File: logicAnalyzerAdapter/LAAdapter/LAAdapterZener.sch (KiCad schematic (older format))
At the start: 13 parts, among them J1 Conn_01x02_Male, J10 Conn_01x01_Female, J2 Conn_01x02_Male, J3 Conn_01x02_Male, J4 Conn_01x02_Male, J5 Conn_02x05_Odd_Even, J6 Conn_01x02_Male, J7 Conn_01x02_Male, J8 Conn_01x02_Male, J9 Conn_01x01_Female

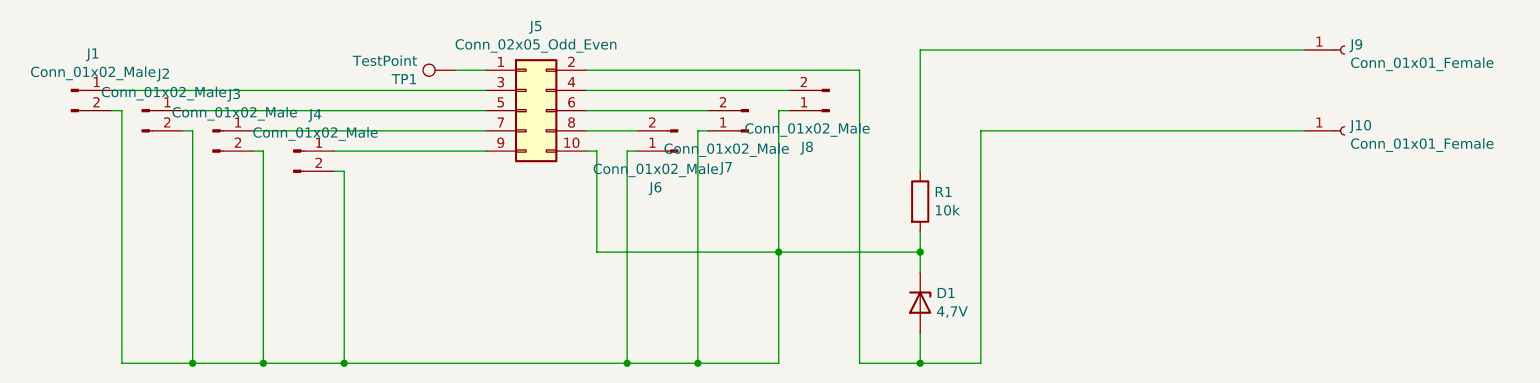
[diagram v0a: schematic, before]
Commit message: opravena hrubá chyba
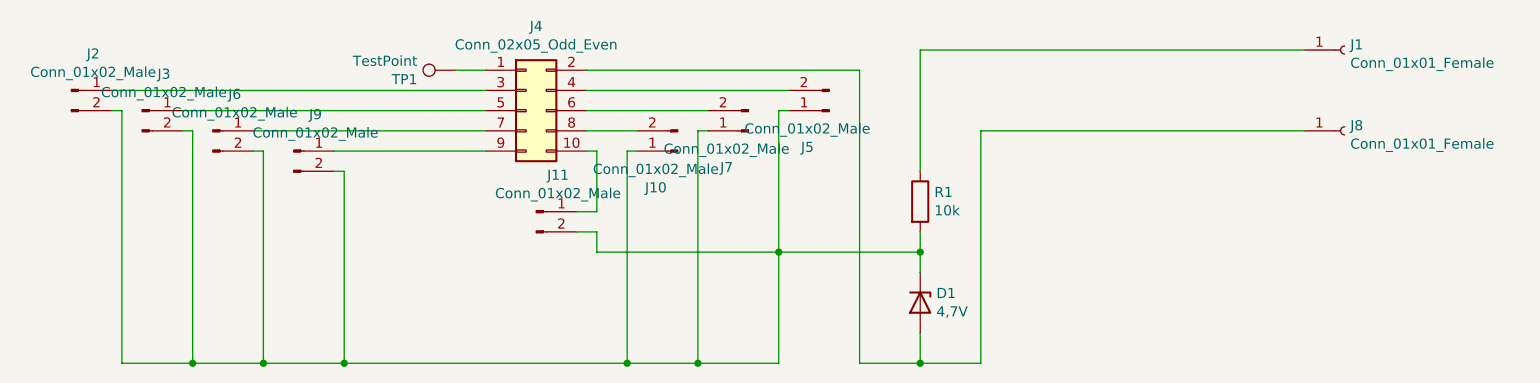
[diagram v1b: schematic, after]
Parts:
- added J11: Conn_01x02_Male, Jumper:SolderJumper-2_P1.3mm_Open_Pad1.0x1.5mm, symbol Connector:Conn_01x02_Male
- J10: renamed from J6; footprint Jumper:SolderJumper-2_P1.3mm_Open_TrianglePad1.0x1.5mm -> Jumper:SolderJumper-2_P1.3mm_Open_Pad1.0x1.5mm
- J2: renamed from J1; footprint Jumper:SolderJumper-2_P1.3mm_Open_TrianglePad1.0x1.5mm -> Jumper:SolderJumper-2_P1.3mm_Open_Pad1.0x1.5mm
- J3: renamed from J2; footprint Jumper:SolderJumper-2_P1.3mm_Open_TrianglePad1.0x1.5mm -> Jumper:SolderJumper-2_P1.3mm_Open_Pad1.0x1.5mm
- J5: renamed from J8; footprint Jumper:SolderJumper-2_P1.3mm_Open_TrianglePad1.0x1.5mm -> Jumper:SolderJumper-2_P1.3mm_Open_Pad1.0x1.5mm
- J6: renamed from J3; footprint Jumper:SolderJumper-2_P1.3mm_Open_TrianglePad1.0x1.5mm -> Jumper:SolderJumper-2_P1.3mm_Open_Pad1.0x1.5mm
- J7: footprint Jumper:SolderJumper-2_P1.3mm_Open_TrianglePad1.0x1.5mm -> Jumper:SolderJumper-2_P1.3mm_Open_Pad1.0x1.5mm
- J9: renamed from J4; footprint Jumper:SolderJumper-2_P1.3mm_Open_TrianglePad1.0x1.5mm -> Jumper:SolderJumper-2_P1.3mm_Open_Pad1.0x1.5mm
- renumbered J9 to J1, J5 to J4, J10 to J8
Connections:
- net at D1.1 (K), J10.1 (Pin_1), J2.2 (Pin_2)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: now also J11.2 (Pin_2); no longer J4.10 (Pin_10)
- new net: J11.1 (Pin_1), J4.10 (Pin_10)
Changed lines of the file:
@@
 $EndComp
 $Comp
-L Connector_Generic:Conn_02x05_Odd_Even J5
+L Connector_Generic:Conn_02x05_Odd_Even J4
 U 1 1 60510CB1
 P 3100 3250
-F 0 "J5" H 3150 3667 50  0000 C CNN
+F 0 "J4" H 3150 3667 50  0000 C CNN
 F 1 "Conn_02x05_Odd_Even" H 3150 3576 50  0000 C CNN
 F 2 "AR_Library:AR_PinHeader_2x05_P2.54mm_Horizontal" H 3100 3250 50  0001 C CNN
@@
 $EndComp
 $Comp
-L Connector:Conn_01x01_Female J10
+L Connector:Conn_01x01_Female J8
 U 1 1 6051A2D4
 P 7150 3350
-F 0 "J10" H 7178 3376 50  0000 L CNN
+F 0 "J8" H 7178 3376 50  0000 L CNN
 F 1 "Conn_01x01_Female" H 7178 3285 50  0000 L CNN
 F 2 "AR_Library:AR_AMASS_4mm_Horizontal" H 7150 3350 50  0001 C CNN
@@
 $EndComp
 $Comp
-L Connector:Conn_01x01_Female J9
+L Connector:Conn_01x01_Female J1
 U 1 1 6051AB13
 P 7150 2950
-F 0 "J9" H 7178 2976 50  0000 L CNN
+F 0 "J1" H 7178 2976 50  0000 L CNN
 F 1 "Conn_01x01_Female" H 7178 2885 50  0000 L CNN
 F 2 "AR_Library:AR_AMASS_4mm_Horizontal" H 7150 2950 50  0001 C CNN
@@
 Wire Wire Line
 	4750 4500 5050 4500
-Wire Wire Line
-	3400 3050 4750 3050
 Connection ~ 5050 4500
 $Comp
-L Connector:Conn_01x02_Male J1
+L Connector:Conn_01x02_Male J2
 U 1 1 60531B24
 P 850 3150
-F 0 "J1" H 958 3331 50  0000 C CNN
+F 0 "J2" H 958 3331 50  0000 C CNN
 F 1 "Conn_01x02_Male" H 958 3240 50  0000 C CNN
-F 2 "Jumper:SolderJumper-2_P1.3mm_Open_TrianglePad1.0x1.5mm" H 850 3150 50  0001 C CNN
+F 2 "Jumper:SolderJumper-2_P1.3mm_Open_Pad1.0x1.5mm" H 850 3150 50  0001 C CNN
 F 3 "~" H 850 3150 50  0001 C CNN
 	1    850  3150
@@
 	5050 3950 5050 4050
 $Comp
-L Connector:Conn_01x02_Male J2
+L Connector:Conn_01x02_Male J3
 U 1 1 60534A19
 P 1200 3250
-F 0 "J2" H 1308 3431 50  0000 C CNN
+F 0 "J3" H 1308 3431 50  0000 C CNN
 F 1 "Conn_01x02_Male" H 1308 3340 50  0000 C CNN
-F 2 "Jumper:SolderJumper-2_P1.3mm_Open_TrianglePad1.0x1.5mm" H 1200 3250 50  0001 C CNN
+F 2 "Jumper:SolderJumper-2_P1.3mm_Open_Pad1.0x1.5mm" H 1200 3250 50  0001 C CNN
 F 3 "~" H 1200 3250 50  0001 C CNN
 	1    1200 3250
@@
 $EndComp
 $Comp
-L Connector:Conn_01x02_Male J3
+L Connector:Conn_01x02_Male J6
 U 1 1 605352E5
 P 1550 3350
-F 0 "J3" H 1658 3531 50  0000 C CNN
+F 0 "J6" H 1658 3531 50  0000 C CNN
 F 1 "Conn_01x02_Male" H 1658 3440 50  0000 C CNN
-F 2 "Jumper:SolderJumper-2_P1.3mm_Open_TrianglePad1.0x1.5mm" H 1550 3350 50  0001 C CNN
+F 2 "Jumper:SolderJumper-2_P1.3mm_Open_Pad1.0x1.5mm" H 1550 3350 50  0001 C CNN
 F 3 "~" H 1550 3350 50  0001 C CNN
 	1    1550 3350
@@
 $EndComp
 $Comp
-L Connector:Conn_01x02_Male J4
+L Connector:Conn_01x02_Male J9
 U 1 1 605396F3
 P 1950 3450
-F 0 "J4" H 2058 3631 50  0000 C CNN
+F 0 "J9" H 2058 3631 50  0000 C CNN
 F 1 "Conn_01x02_Male" H 2058 3540 50  0000 C CNN
-F 2 "Jumper:SolderJumper-2_P1.3mm_Open_TrianglePad1.0x1.5mm" H 1950 3450 50  0001 C CNN
+F 2 "Jumper:SolderJumper-2_P1.3mm_Open_Pad1.0x1.5mm" H 1950 3450 50  0001 C CNN
 F 3 "~" H 1950 3450 50  0001 C CNN
 	1    1950 3450
@@
 	3400 3450 3450 3450
 Wire Wire Line
-	3450 3450 3450 3950
-Wire Wire Line
 	3450 3950 4350 3950
 $Comp
-L Connector:Conn_01x02_Male J8
+L Connector:Conn_01x02_Male J5
 U 1 1 6053DACB
 P 4600 3250
-F 0 "J8" H 4708 3431 50  0000 C CNN
+F 0 "J5" H 4708 3431 50  0000 C CNN
 F 1 "Conn_01x02_Male" H 4708 3340 50  0000 C CNN
-F 2 "Jumper:SolderJumper-2_P1.3mm_Open_TrianglePad1.0x1.5mm" H 4600 3250 50  0001 C CNN
+F 2 "Jumper:SolderJumper-2_P1.3mm_Open_Pad1.0x1.5mm" H 4600 3250 50  0001 C CNN
 F 3 "~" H 4600 3250 50  0001 C CNN
 	1    4600 3250
@@
 F 0 "J7" H 4308 3531 50  0000 C CNN
 F 1 "Conn_01x02_Male" H 4308 3440 50  0000 C CNN
-F 2 "Jumper:SolderJumper-2_P1.3mm_Open_TrianglePad1.0x1.5mm" H 4200 3350 50  0001 C CNN
+F 2 "Jumper:SolderJumper-2_P1.3mm_Open_Pad1.0x1.5mm" H 4200 3350 50  0001 C CNN
 F 3 "~" H 4200 3350 50  0001 C CNN
 	1    4200 3350
@@
 $EndComp
 $Comp
-L Connector:Conn_01x02_Male J6
+L Connector:Conn_01x02_Male J10
 U 1 1 6053F0C1
 P 3850 3450
-F 0 "J6" H 3958 3631 50  0000 C CNN
+F 0 "J10" H 3958 3631 50  0000 C CNN
 F 1 "Conn_01x02_Male" H 3958 3540 50  0000 C CNN
-F 2 "Jumper:SolderJumper-2_P1.3mm_Open_TrianglePad1.0x1.5mm" H 3850 3450 50  0001 C CNN
+F 2 "Jumper:SolderJumper-2_P1.3mm_Open_Pad1.0x1.5mm" H 3850 3450 50  0001 C CNN
 F 3 "~" H 3850 3450 50  0001 C CNN
 	1    3850 3450
@@
 Wire Wire Line
 	4350 3950 4350 4500
+Wire Wire Line
+	3400 3050 4750 3050
+$Comp
+L Connector:Conn_01x02_Male J11
+U 1 1 6051475B
+P 3150 3750
+F 0 "J11" H 3258 3931 50  0000 C CNN
+F 1 "Conn_01x02_Male" H 3258 3840 50  0000 C CNN
+F 2 "Jumper:SolderJumper-2_P1.3mm_Open_Pad1.0x1.5mm" H 3150 3750 50  0001 C CNN
+F 3 "~" H 3150 3750 50  0001 C CNN
+	1    3150 3750
+	1    0    0    -1
+$EndComp
+Wire Wire Line
+	3450 3950 3450 3850
+Wire Wire Line
+	3450 3850 3350 3850
+Wire Wire Line
+	3350 3750 3450 3750
+Wire Wire Line
+	3450 3750 3450 3450
 $EndSCHEMATC
